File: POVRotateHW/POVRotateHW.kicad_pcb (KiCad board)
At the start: 2 copper layers, 57 parts, among them P1 CONN_01X02, P2 CONN_01X05, U1 A5970AD, U10 APA102C, U11 APA102C, U12 APA102C, U2 M24M01, U3 LMC6062, U4 CYBLE-022001-00, U5 APA102C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

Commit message: Moved parts around.
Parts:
- removed the C8 at (165.1, 138.4)
- moved R13 91.9 mm to (132.1, 83.8), turned to 270 degrees
- moved R10 85.8 mm to (132.1, 88.9), turned to 270 degrees
- moved R12 75.0 mm to (144.8, 88.9), turned to 90 degrees
- moved R11 56.4 mm to (141.0, 81.3), turned to 180 degrees
- moved R3 37.0 mm to (148.6, 146.1), turned to 270 degrees
- moved L1 31.9 mm to (171.4, 147.3)
- moved R2 28.2 mm to (152.4, 138.4), turned to 180 degrees
- moved R4 26.8 mm to (148.6, 141.0), turned to 90 degrees
- moved D5 26.2 mm to (165.1, 167.6)
- moved R1 26.1 mm to (156.2, 167.6)
- moved R7 23.4 mm to (170.2, 119.4), turned to 90 degrees
- moved C8 23.3 mm to (174.0, 156.2), turned to 270 degrees
- moved C7 23.0 mm to (177.8, 156.2), turned to 270 degrees
- moved W3 21.3 mm to (180.3, 149.9)
- moved C4 18.9 mm to (152.4, 151.1), turned to 270 degrees
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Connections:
- P1 pad 1: /Power/12V -> PWR
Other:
- board outline added: 61 x 190.5 mm

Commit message: Working on PCB placement.
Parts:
- added REF**: 1pin, Connect:1pin, F.Cu at (188.0, 52.0)
- added REF**: 1pin, Connect:1pin, F.Cu at (188.0, 240.0)
- moved R13 141.0 mm to (195.0, 210.0), turned to 90 degrees
- moved R11 139.9 mm to (188.0, 213.0), turned to 0 degrees
- moved R10 131.2 mm to (195.0, 204.0), turned to 90 degrees
- moved U3 126.2 mm to (188.0, 205.0), turned to 180 degrees
- moved C10 122.8 mm to (198.0, 198.0), turned to 90 degrees
- moved R12 120.5 mm to (180.2, 204.1), turned to 270 degrees
- moved R9 119.8 mm to (195.0, 198.0), turned to 90 degrees
- moved D7 111.8 mm to (188.0, 198.0), turned to 180 degrees
- moved C3 66.6 mm to (204.0, 231.0)
- moved R1 58.9 mm to (179.0, 222.0)
- moved D5 58.9 mm to (190.0, 221.0)
- moved C2 57.6 mm to (172.0, 231.0)
- moved D3 50.9 mm to (182.0, 228.0)
- moved D1 50.6 mm to (182.0, 234.0)
- moved D4 50.5 mm to (194.0, 228.0)
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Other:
- board size 61 x 190.5 mm -> 46 x 196 mm

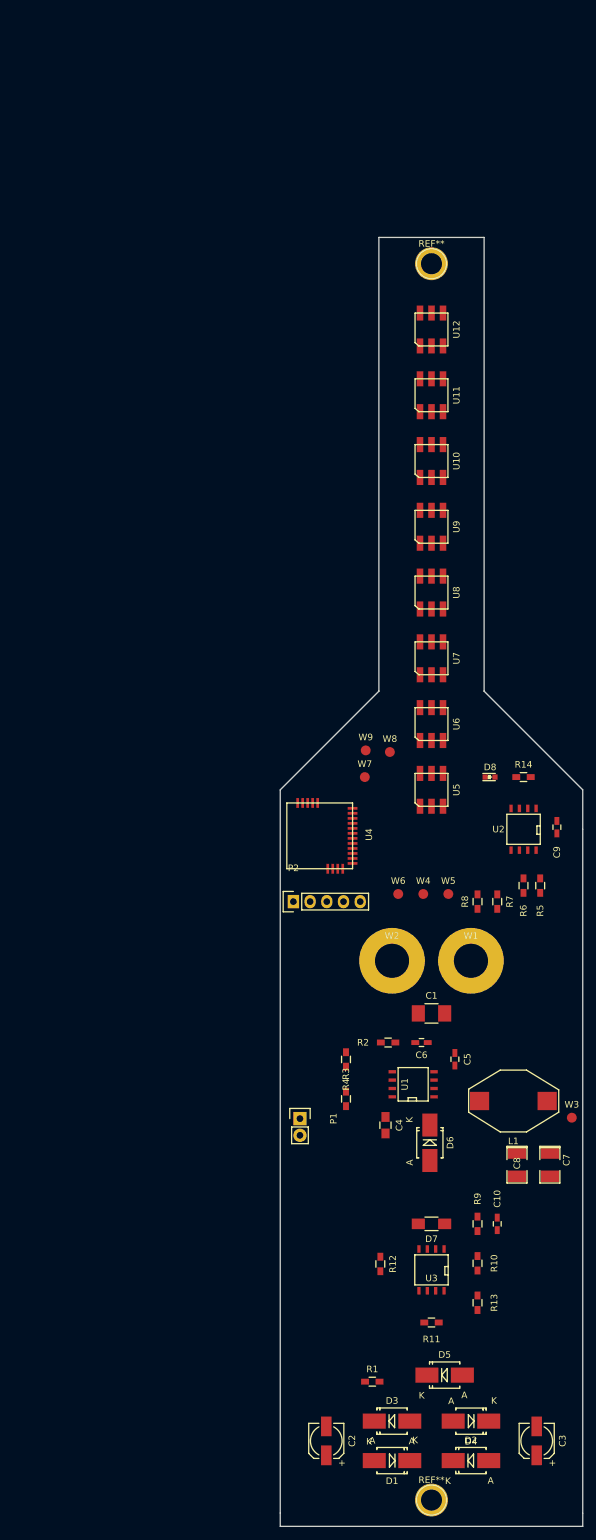
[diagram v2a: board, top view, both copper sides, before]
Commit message: Updated the designs ref des to the LEDs work.
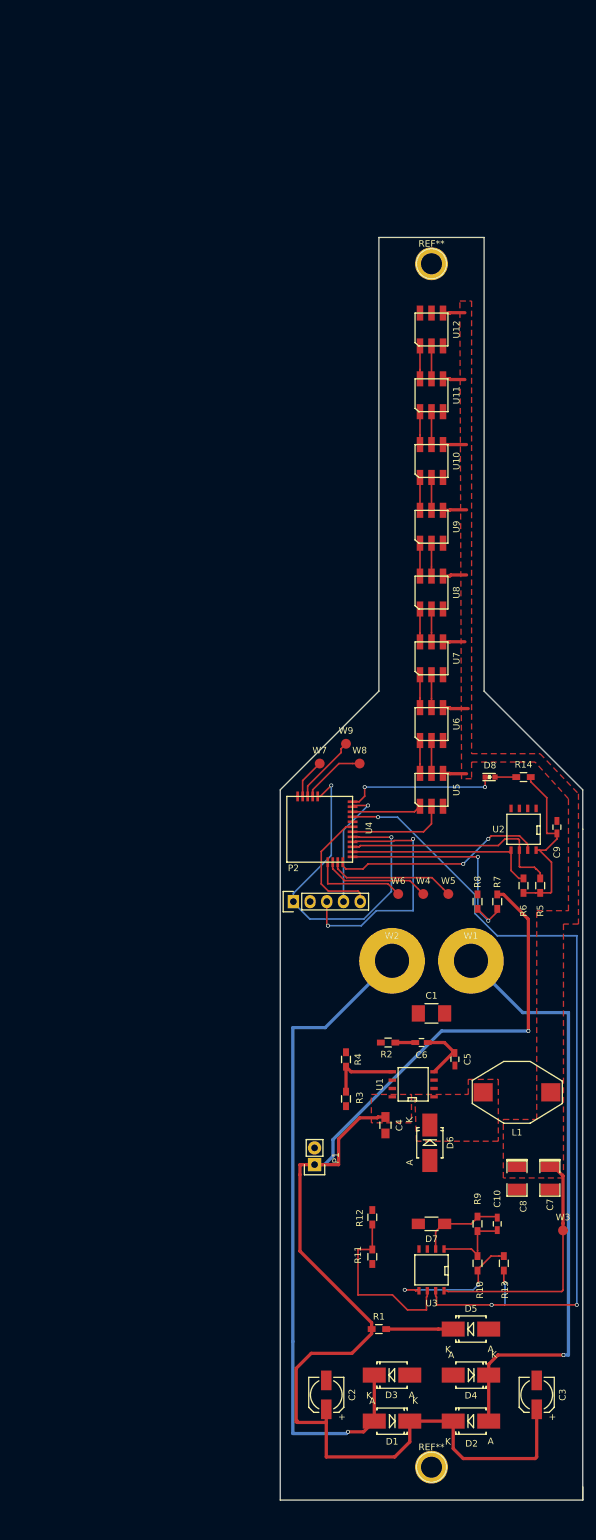
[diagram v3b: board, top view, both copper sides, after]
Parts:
- moved W3 17.2 mm to (208.0, 199.0)
- moved R11 13.5 mm to (179.0, 203.0), turned to 270 degrees
- moved D5 8.06 mm to (194.0, 214.0)
- moved R1 8.06 mm to (180.0, 214.0)
- moved P1 7.33 mm to (170.2, 189.0), turned to 90 degrees
- moved R13 7.21 mm to (199.0, 204.0)
- moved R12 7.20 mm to (179.0, 197.0)
- moved W7 7.16 mm to (171.0, 128.0)
- moved C2 7.00 mm to (172.0, 224.0)
- moved C3 7.00 mm to (204.0, 224.0)
- moved D3 7.00 mm to (182.0, 221.0)
- moved D4 7.00 mm to (194.0, 221.0)
- moved D1 6.00 mm to (182.0, 228.0)
- moved D2 6.00 mm to (194.0, 228.0)
- moved REF** 5.00 mm to (188.0, 235.0)
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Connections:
- U11 pad 1: Net-(U11-Pad1) -> Net-(U10-Pad6)
- U11 pad 2: Net-(U11-Pad2) -> Net-(U10-Pad5)
- U12 pad 1: Net-(U10-Pad6) -> Net-(U11-Pad6)
- U12 pad 2: Net-(U10-Pad5) -> Net-(U11-Pad5)
- U6 pad 1: Net-(U11-Pad6) -> Net-(U5-Pad6)
- U6 pad 2: Net-(U11-Pad5) -> Net-(U5-Pad5)
- U7 pad 1: Net-(U5-Pad6) -> Net-(U6-Pad6)
- U7 pad 2: Net-(U5-Pad5) -> Net-(U6-Pad5)
- U8 pad 1: Net-(U6-Pad6) -> Net-(U7-Pad6)
- U8 pad 2: Net-(U6-Pad5) -> Net-(U7-Pad5)
- U8 pad 5: Net-(U10-Pad2) -> Net-(U8-Pad5)
- U8 pad 6: Net-(U10-Pad1) -> Net-(U8-Pad6)
- U9 pad 1: Net-(U7-Pad6) -> Net-(U8-Pad6)
- U9 pad 2: Net-(U7-Pad5) -> Net-(U8-Pad5)
- U9 pad 5: Net-(U11-Pad2) -> Net-(U10-Pad2)
- U9 pad 6: Net-(U11-Pad1) -> Net-(U10-Pad1)
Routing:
- net PWR: track 0.00 -> 196.5 mm, vias 0 -> 1
- net VCC: track 0.00 -> 148.7 mm, vias 0 -> 2
- net /BLE/ALIGNMENT: track 0.00 -> 130.3 mm, vias 0 -> 4
- net Net-(C1-Pad1): track 0.00 -> 101.2 mm, vias 0 -> 1
- net Net-(C1-Pad2): track 0.00 -> 91.9 mm, vias 0 -> 1
- net /BLE/XRES: track 0.00 -> 38.0 mm, vias 0 -> 2
- net /BLE/SCL: track 0.00 -> 34.4 mm
- net /BLE/INPUT_POWER: track 0.00 -> 34.3 mm, vias 0 -> 2
- net /BLE/WP: track 0.00 -> 32.7 mm, vias 0 -> 2
- net /BLE/SDA: track 0.00 -> 29.7 mm
- net Net-(R11-Pad1): track 0.00 -> 27.2 mm
- net /BLE/LED: track 0.00 -> 23.4 mm, vias 0 -> 2
- net Net-(R10-Pad1): track 0.00 -> 20.9 mm, vias 0 -> 2
- net /BLE/TX: track 0.00 -> 19.4 mm
- net /BLE/SWDIO: track 0.00 -> 19.0 mm
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- added copper zone on F.Cu, net Net-(D6-Pad1)
- added copper zone on F.Cu, net PWR
- added copper zone on F.Cu, net VCC
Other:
- board size 46 x 196 mm -> 46 x 192 mm
- net class PWR added: clearance 0.2, trace_width 0.5, via_dia 0.6, via_drill 0.4

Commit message: Finished routing board. Need to do another once over.
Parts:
- added REF**: via_0.3mm, KicadLibrary:via_0.3mm, F.Cu at (171.0, 181.0)
- added REF**: via_0.3mm, KicadLibrary:via_0.3mm, F.Cu at (194.0, 137.0)
- added REF**: via_0.3mm, KicadLibrary:via_0.3mm, F.Cu at (179.0, 187.0)
- added REF**: via_0.3mm, KicadLibrary:via_0.3mm, F.Cu at (180.0, 124.0)
- added REF**: via_0.3mm, KicadLibrary:via_0.3mm, F.Cu at (197.0, 124.0)
- added REF**: via_0.3mm, KicadLibrary:via_0.3mm, F.Cu at (198.0, 144.0)
- added REF**: via_0.3mm, KicadLibrary:via_0.3mm, F.Cu at (179.0, 137.0)
- added REF**: via_0.3mm, KicadLibrary:via_0.3mm, F.Cu at (167.5, 131.0)
- added REF**: via_0.3mm, KicadLibrary:via_0.3mm, F.Cu at (175.0, 132.0)
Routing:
- net VCC: track 148.7 -> 191.8 mm
- net Net-(C1-Pad1): track 101.2 -> 112.6 mm
- net Net-(C1-Pad2): track 91.9 -> 103.3 mm
- net GND: track 0.00 -> 3.06 mm
- added copper zone on B.Cu, net GND
- added copper zone on F.Cu, net GND

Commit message: Updated the 3D shapes. Debating if I should try and squish the design into a smaller form factor.
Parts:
- added REF**: via_0.3mm, KicadLibrary:via_0.3mm, F.Cu at (201.2, 155.8)
- added REF**: via_0.3mm, KicadLibrary:via_0.3mm, F.Cu at (188.2, 151.2)
- added REF**: via_0.3mm, KicadLibrary:via_0.3mm, F.Cu at (197.8, 166.0)

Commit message: Added silk screen.
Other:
- board text added: "POV Rotate Rev A Nick Butts Copyright 2016"
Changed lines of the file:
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@@
     (links 136)
     (no_connects 3)
-    (area 164.924999 47.924999 211.075001 240.075001)
+    (area 163.32381 47.924999 211.075001 240.075001)
     (thickness 1.6)
-    (drawings 10)
+    (drawings 11)
     (tracks 337)
     (zones 0)
@@
       (net 4 GND) (zone_connect 2))
   )
+  (gr_text "POV Rotate Rev A\nNick Butts\nCopyright 2016" (at 188.75 192.75) (layer B.SilkS)
+    (effects (font (size 1.5 1.5) (thickness 0.3)) (justify mirror))
+  )
   (gr_line (start 165 240) (end 211 240) (angle 90) (layer Edge.Cuts) (width 0.15))

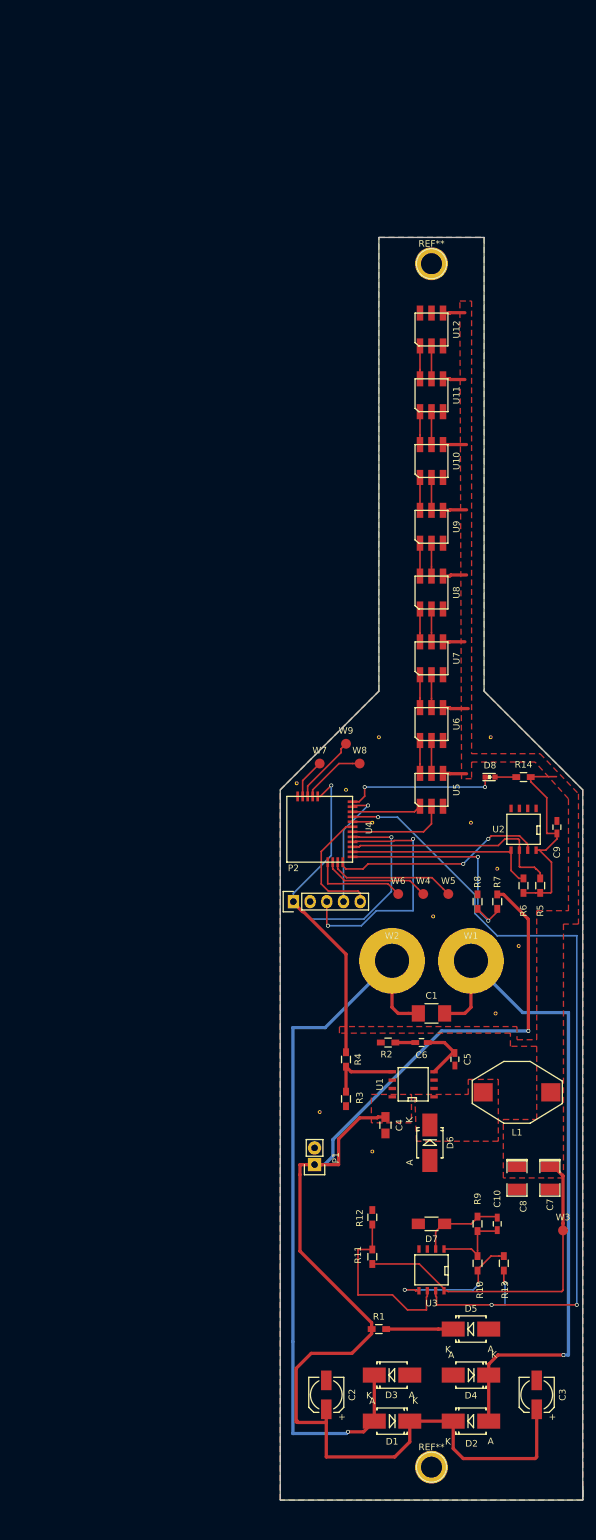
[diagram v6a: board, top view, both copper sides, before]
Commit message: Rerouting board for RevB
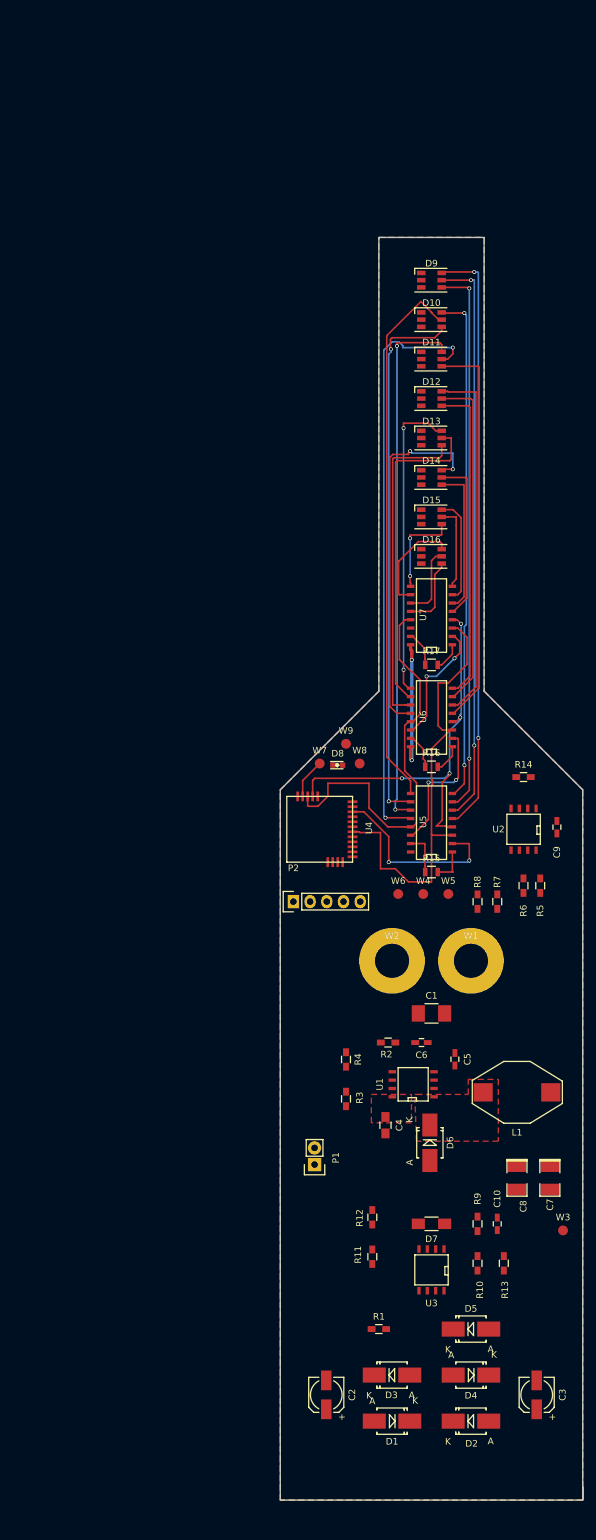
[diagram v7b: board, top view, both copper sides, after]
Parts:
- removed REF** (x12): via_0.3mm, KicadLibrary:via_0.3mm
- removed REF** (x2): 1pin, Connect:1pin
- removed U10, U11, U12, U8, U9: APA102C, KicadLibrary:LED_5050
- added D10: LED_RGB, LEDs:LED_RGB_PLLC-6, F.Cu at (188.0, 60.5)
- added D11: LED_RGB, LEDs:LED_RGB_PLLC-6, F.Cu at (188.0, 66.5)
- added D12: LED_RGB, LEDs:LED_RGB_PLLC-6, F.Cu at (188.0, 72.5)
- added D13: LED_RGB, LEDs:LED_RGB_PLLC-6, F.Cu at (188.0, 78.5)
- added D14: LED_RGB, LEDs:LED_RGB_PLLC-6, F.Cu at (188.0, 84.5)
- added D15: LED_RGB, LEDs:LED_RGB_PLLC-6, F.Cu at (188.0, 90.5)
- added D16: LED_RGB, LEDs:LED_RGB_PLLC-6, F.Cu at (188.0, 96.5)
- added D9: LED_RGB, LEDs:LED_RGB_PLLC-6, F.Cu at (188.0, 54.5)
- added R15: 1K, Resistors_SMD:R_0805, F.Cu at (188.0, 144.5)
- added R16: 1K, Resistors_SMD:R_0805, F.Cu at (188.0, 128.5)
- added R17: 1K, Resistors_SMD:R_0805, F.Cu at (188.0, 113.0)
- R8: value 700k -> 1M
- U5, U6, U7: value APA102C -> STP08DP05; footprint KicadLibrary:LED_5050 -> SMD_Packages:SO-16-N
- moved D8 23.2 mm to (173.8, 128.2)
- moved U7 6.50 mm to (188.0, 105.5)
- moved U5 5.00 mm to (188.0, 137.0)
- moved U6 1.00 mm to (188.0, 121.0)
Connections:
- U4 pad 3: Net-(U4-Pad3) -> OE
- U4 pad 4: Net-(U4-Pad4) -> LE
- U5 pad 1: MOSI -> GND
- U5 pad 2: SCLK -> MOSI
- U5 pad 3: GND -> SCLK
- U5 pad 4: VCC -> LE
- U5 pad 5: Net-(U5-Pad5) -> Net-(D9-Pad6)
- U5 pad 6: Net-(U5-Pad6) -> Net-(D9-Pad5)
- U6 pad 1: Net-(U5-Pad6) -> GND
- U6 pad 2: Net-(U5-Pad5) -> Net-(U5-Pad14)
- U6 pad 3: GND -> SCLK
- U6 pad 4: VCC -> LE
- U6 pad 5: Net-(U6-Pad5) -> Net-(D11-Pad4)
- U6 pad 6: Net-(U6-Pad6) -> Net-(D12-Pad6)
- U7 pad 1: Net-(U6-Pad6) -> GND
- U7 pad 2: Net-(U6-Pad5) -> Net-(U6-Pad14)
- U7 pad 3: GND -> SCLK
- U7 pad 4: VCC -> LE
- W8 pad 1: Net-(U4-Pad4) -> LE
- W9 pad 1: Net-(U4-Pad3) -> OE
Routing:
- net PWR: track 196.5 -> 0.00 mm, vias 1 -> 0
- net VCC: track 191.8 -> 19.8 mm
- net /BLE/ALIGNMENT: track 130.3 -> 0.00 mm, vias 4 -> 0
- net Net-(C1-Pad1): track 112.6 -> 0.00 mm, vias 1 -> 0
- net Net-(C1-Pad2): track 103.3 -> 0.00 mm, vias 1 -> 0
- net Net-(D9-Pad6): track 0.00 -> 90.8 mm, vias 0 -> 2
- net Net-(D11-Pad5): track 0.00 -> 89.6 mm, vias 0 -> 2
- net Net-(D9-Pad5): track 0.00 -> 87.4 mm, vias 0 -> 2
- net Net-(D9-Pad4): track 0.00 -> 83.9 mm, vias 0 -> 2
- net Net-(D10-Pad5): track 0.00 -> 82.8 mm
- net Net-(D10-Pad4): track 0.00 -> 82.7 mm, vias 0 -> 2
- net Net-(D11-Pad6): track 0.00 -> 81.5 mm, vias 0 -> 2
- net Net-(D10-Pad6): track 0.00 -> 77.7 mm, vias 0 -> 2
- net LE: track 0.00 -> 61.5 mm, vias 0 -> 4
- net OE: track 0.00 -> 61.3 mm
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- removed copper zone on F.Cu, net VCC

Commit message: Starting layout on the new design.
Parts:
- removed P1: CONN_01X02, Socket_Strips:Socket_Strip_Straight_1x02
- removed U6, U7: STP08DP05, SMD_Packages:SO-16-N
- added W10: TEST_1P, Measurement_Points:Measurement_Point_Round-SMD-Pad_Small, F.Cu at (177.0, 127.5)
- added W11: TEST_1P, Measurement_Points:Measurement_Point_Round-SMD-Pad_Small, F.Cu at (182.0, 126.0)
- added W12: TEST_1P, Measurement_Points:Measurement_Point_Round-SMD-Pad_Small, F.Cu at (202.0, 130.0)
- added W13: TEST_1P, Measurement_Points:Measurement_Point_Round-SMD-Pad_Small, F.Cu at (172.5, 187.5)
- added W14: TEST_1P, Measurement_Points:Measurement_Point_Round-SMD-Pad_Small, F.Cu at (175.5, 191.5)
- D10, D11, D12, D13, D14, D15, D16, D9: value LED_RGB -> LED_RABG; footprint LEDs:LED_RGB_PLLC-6 -> KicadFootprint:CREE_PLCC4
- U5: value STP08DP05 -> STP24DP05; footprint SMD_Packages:SO-16-N -> Housings_QFP:TQFP-48_7x7mm_Pitch0.5mm
- W7: value P4.1 -> TEST_1P
- W8: value P5.0 -> TEST_1P
- W9: value P5.1 -> TEST_1P
- moved C3 60.5 mm to (170.0, 174.0), turned to 0 degrees
- moved C2 42.5 mm to (170.0, 181.5), turned to 0 degrees
- moved C9 38.5 mm to (173.1, 155.7)
- moved R5 38.5 mm to (170.5, 164.6)
- moved R6 38.5 mm to (168.0, 164.6)
- moved U2 37.6 mm to (169.0, 156.0)
- moved W3 33.0 mm to (208.0, 166.0)
- moved R17 31.6 mm to (206.0, 139.0)
- moved D9 28.5 mm to (188.0, 83.0)
- moved D10 27.5 mm to (188.0, 88.0)
- moved D11 26.5 mm to (188.0, 93.0)
- moved D12 25.5 mm to (188.0, 98.0)
- moved D13 24.5 mm to (188.0, 103.0)
- moved W9 24.0 mm to (198.0, 132.0)
- moved R14 24.0 mm to (178.0, 131.0)
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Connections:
- D10 pad 1: GND -> Net-(D10-Pad1)
- D10 pad 2: GND -> VCC
- D10 pad 3: GND -> Net-(D10-Pad3)
- D11 pad 1: GND -> Net-(D11-Pad1)
- D11 pad 2: GND -> VCC
- D11 pad 3: GND -> Net-(D11-Pad3)
- D12 pad 1: GND -> Net-(D12-Pad1)
- D12 pad 2: GND -> VCC
- D12 pad 3: GND -> Net-(D12-Pad3)
- D13 pad 1: GND -> Net-(D13-Pad1)
- D13 pad 2: GND -> VCC
- D13 pad 3: GND -> Net-(D13-Pad3)
- D14 pad 1: GND -> Net-(D14-Pad1)
- D14 pad 2: GND -> VCC
- D14 pad 3: GND -> Net-(D14-Pad3)
- D15 pad 1: GND -> Net-(D15-Pad1)
- D15 pad 2: GND -> VCC
- D15 pad 3: GND -> Net-(D15-Pad3)
- D16 pad 1: GND -> Net-(D16-Pad1)
- D16 pad 2: GND -> VCC
- D16 pad 3: GND -> Net-(D16-Pad3)
- D9 pad 1: GND -> Net-(D9-Pad1)
- D9 pad 2: GND -> VCC
- D9 pad 3: GND -> Net-(D9-Pad3)
- U1 pad 2: Net-(U1-Pad2) -> (no net)
- U1 pad 6: Net-(U1-Pad6) -> (no net)
- U2 pad 1: Net-(U2-Pad1) -> (no net)
- U4 pad 2: Net-(U4-Pad2) -> DG
- U5 pad 10: Net-(D10-Pad4) -> VCC
- U5 pad 11: Net-(D11-Pad6) -> VCC
- U5 pad 12: Net-(D11-Pad5) -> GND
- U5 pad 13: OE -> Net-(D9-Pad1)
- U5 pad 14: Net-(U5-Pad14) -> Net-(D9-Pad4)
- U5 pad 15: Net-(R15-Pad1) -> Net-(D9-Pad3)
- U5 pad 16: VCC -> Net-(D10-Pad1)
- U5 pad 3: SCLK -> LE
- U5 pad 4: LE -> SCLK
- U5 pad 5: Net-(D9-Pad6) -> VCC
- U5 pad 6: Net-(D9-Pad5) -> VCC
- U5 pad 7: Net-(D9-Pad4) -> GND
- U5 pad 8: Net-(D10-Pad6) -> Net-(U5-Pad8)
- U5 pad 9: Net-(D10-Pad5) -> DG
- W7 pad 1: Net-(U4-Pad2) -> VCC
- W8 pad 1: LE -> Net-(U5-Pad8)
- W9 pad 1: OE -> Net-(U5-Pad29)
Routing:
- net Net-(D9-Pad6): track 90.8 -> 0.00 mm, vias 2 -> 0
- net Net-(D11-Pad5): track 89.6 -> 0.00 mm, vias 2 -> 0
- net Net-(D9-Pad5): track 87.4 -> 0.00 mm, vias 2 -> 0
- net Net-(D9-Pad4): track 83.9 -> 0.00 mm, vias 2 -> 0
- net Net-(D10-Pad5): track 82.8 -> 0.00 mm
- net Net-(D10-Pad4): track 82.7 -> 0.00 mm, vias 2 -> 0
- net Net-(D11-Pad6): track 81.5 -> 0.00 mm, vias 2 -> 0
- net Net-(D10-Pad6): track 77.7 -> 0.00 mm, vias 2 -> 0
- net SCLK: track 68.1 -> 0.00 mm
- net LE: track 61.5 -> 0.00 mm, vias 4 -> 0
- net OE: track 61.3 -> 0.00 mm
- net Net-(D11-Pad4): track 60.2 -> 0.00 mm
- net Net-(D14-Pad6): track 55.9 -> 0.00 mm, vias 2 -> 0
- net Net-(D12-Pad6): track 54.8 -> 0.00 mm
- net Net-(D12-Pad5): track 51.3 -> 0.00 mm
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- removed copper zone on B.Cu, net GND
- removed copper zone on F.Cu, net GND
- removed copper zone on F.Cu, net Net-(D6-Pad1)
- removed copper zone on F.Cu, net PWR
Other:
- board size 46 x 192 mm -> 46 x 158 mm
